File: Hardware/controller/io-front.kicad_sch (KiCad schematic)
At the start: 35 parts

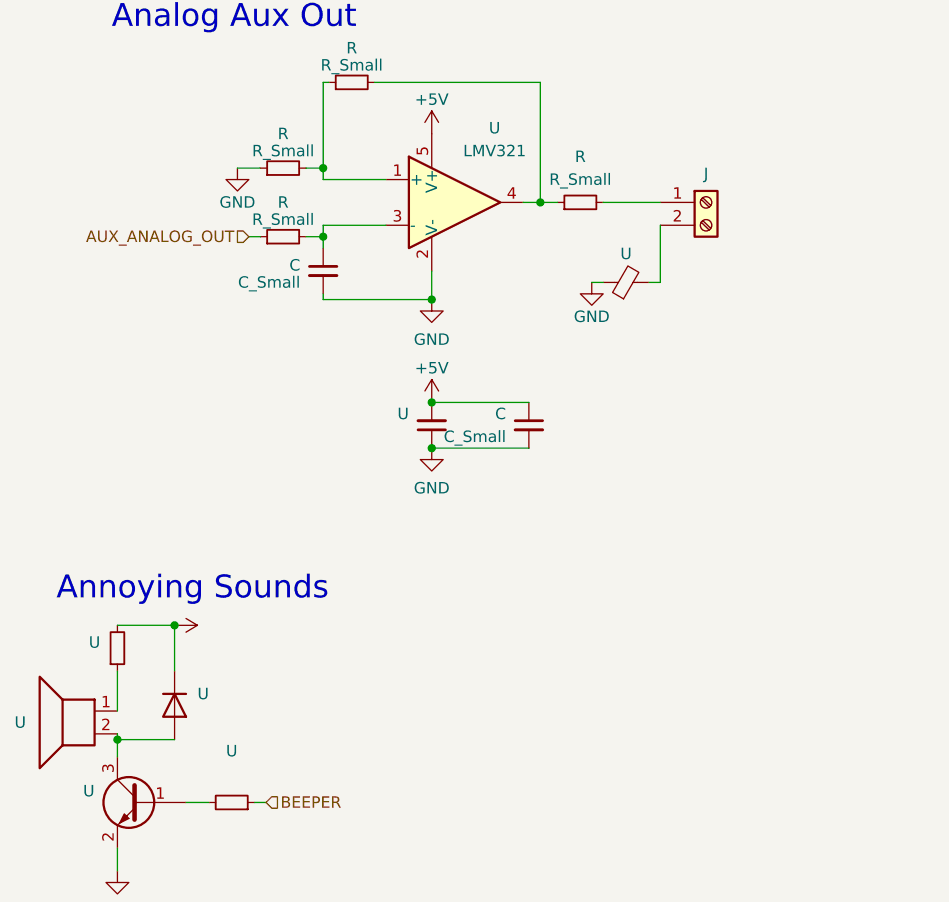
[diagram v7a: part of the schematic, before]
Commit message: hw: add more jlcpcb part numbers
- Switched a lot more passives around to use equivalent JLCPCB-available
  parts

- Slightly moved expansion power relay
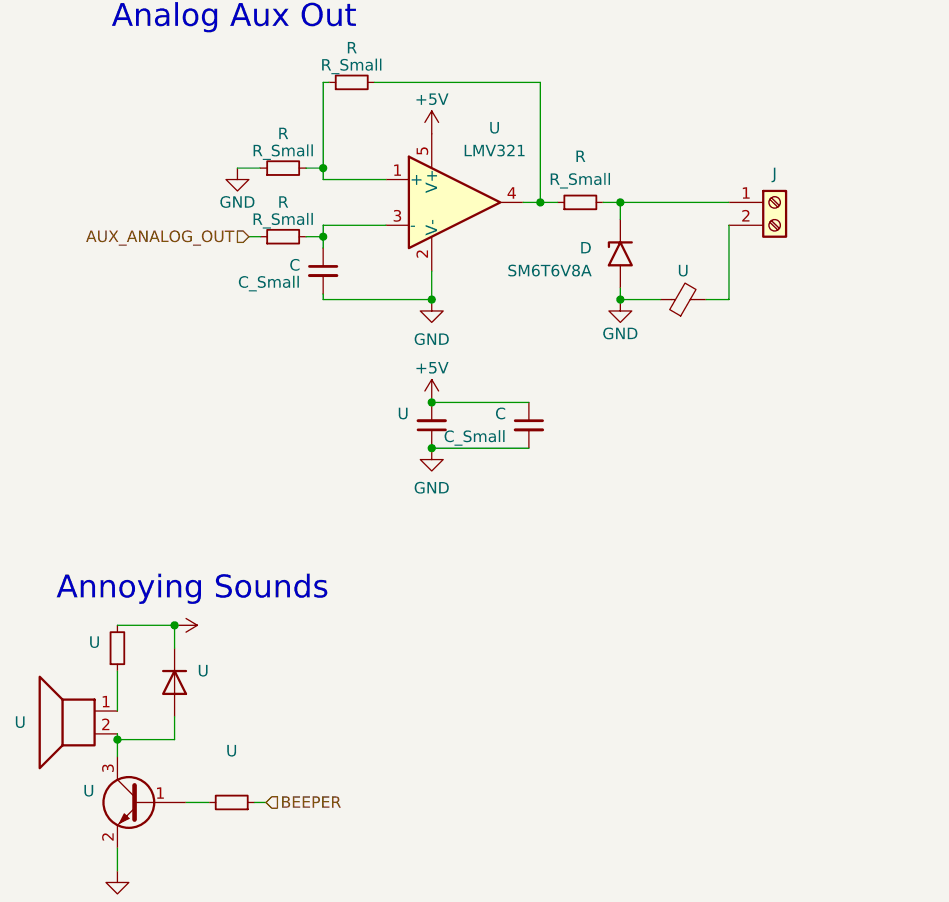
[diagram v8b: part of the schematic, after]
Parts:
- added D: SM6T6V8A, Diode_SMD:D_SMB, symbol Diode:SM6T6V8A
- U: MPN (none) -> CR0805-JW-102ELF
- U: JLCPCB (none) -> C64898; MPN FM4007W-W -> (none)
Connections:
- net GND: now also D.2 (A2)
- net at J.1 (Pin_1), R.2: now also D.1 (A1)
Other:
- moved on the sheet: J, U
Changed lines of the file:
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@@
   (junction (at 31.75 173.355) (diameter 0) (color 0 0 0 0)
+  )
+  (junction (at 164.465 125.095) (diameter 0) (color 0 0 0 0)
+  )
+  (junction (at 164.465 114.3) (diameter 0) (color 0 0 0 0)
   )
   (junction (at 114.935 161.29) (diameter 0) (color 0 0 0 0)
@@
     (stroke (width 0) (type default))
   )
-  (wire (pts (xy 168.91 116.84) (xy 168.91 123.19))
-    (stroke (width 0) (type default))
-  )
   (wire (pts (xy 131.445 111.76) (xy 131.445 110.49))
     (stroke (width 0) (type default))
@@
     (stroke (width 0) (type default))
   )
+  (wire (pts (xy 176.53 116.84) (xy 176.53 125.095))
+    (stroke (width 0) (type default))
+  )
   (wire (pts (xy 40.005 181.61) (xy 52.705 181.61))
     (stroke (width 0) (type default))
   )
+  (wire (pts (xy 162.56 114.3) (xy 164.465 114.3))
+    (stroke (width 0) (type default))
+  )
   (wire (pts (xy 31.75 173.355) (xy 31.75 165.1))
     (stroke (width 0) (type default))
   )
+  (wire (pts (xy 164.465 114.3) (xy 176.53 114.3))
+    (stroke (width 0) (type default))
+  )
   (bus (pts (xy 89.535 68.58) (xy 89.535 71.12))
     (stroke (width 0) (type default))
@@
     (stroke (width 0) (type default))
   )
+  (wire (pts (xy 168.91 125.095) (xy 164.465 125.095))
+    (stroke (width 0) (type default))
+  )
   (bus (pts (xy 89.535 48.26) (xy 89.535 50.8))
     (stroke (width 0) (type default))
@@
     (stroke (width 0) (type default))
   )
-  (wire (pts (xy 162.56 114.3) (xy 168.91 114.3))
-    (stroke (width 0) (type default))
-  )
   (wire (pts (xy 31.75 150.495) (xy 31.75 165.1))
     (stroke (width 0) (type default))
   )
-  (wire (pts (xy 168.91 123.19) (xy 167.64 123.19))
+  (wire (pts (xy 173.99 125.095) (xy 176.53 125.095))
     (stroke (width 0) (type default))
   )
@@
     (stroke (width 0) (type default))
   )
+  (wire (pts (xy 164.465 114.3) (xy 164.465 116.205))
+    (stroke (width 0) (type default))
+  )
   (wire (pts (xy 132.08 100.965) (xy 131.445 100.965))
     (stroke (width 0) (type default))
@@
     (stroke (width 0) (type default))
   )
+  (wire (pts (xy 114.935 171.45) (xy 114.935 173.99))
+    (stroke (width 0) (type default))
+  )
   (bus (pts (xy 89.535 83.82) (xy 89.535 86.36))
     (stroke (width 0) (type default))
@@
     (stroke (width 0) (type default))
   )
+  (wire (pts (xy 164.465 125.095) (xy 164.465 123.825))
+    (stroke (width 0) (type default))
+  )
   (bus (pts (xy 89.535 45.72) (xy 89.535 48.26))
     (stroke (width 0) (type default))
@@
     (stroke (width 0) (type default))
   )
-  (wire (pts (xy 161.29 123.19) (xy 162.56 123.19))
-    (stroke (width 0) (type default))
-  )
   (wire (pts (xy 139.7 36.83) (xy 165.1 36.83))
     (stroke (width 0) (type default))
@@
     (stroke (width 0) (type default))
   )
-  (wire (pts (xy 114.935 161.29) (xy 114.935 166.37))
+  (wire (pts (xy 114.935 161.29) (xy 114.935 163.83))
     (stroke (width 0) (type default))
   )
@@
       (effects (font (size 1.27 1.27)) hide)
     )
-    (property "MPN" "" (id 4) (at 221.615 33.655 0)
+    (property "MPN" "CR0805-JW-102ELF" (id 4) (at 221.615 33.655 0)
       (effects (font (size 1.27 1.27)) hide)
     )
@@
     (pin "2")
   )
-  (symbol (lib_id "Device:FerriteBead_Small") (at 165.1 123.19 90) (unit 1)
+  (symbol (lib_id "Device:FerriteBead_Small") (at 171.45 125.095 90) (unit 1)
     (in_bom yes) (on_board yes)
     (default_instance (reference "U") (unit 1) (value "") (footprint ""))
-    (property "Reference" "U" (id 0) (at 165.1 120.015 90)
-      (effects (font (size 1.27 1.27)))
-    )
-    (property "Value" "" (id 1) (at 165.0619 118.745 90)
-      (effects (font (size 1.27 1.27)) hide)
-    )
-    (property "Footprint" "" (id 2) (at 165.1 124.968 90)
-      (effects (font (size 1.27 1.27)) hide)
-    )
-    (property "Datasheet" "~" (id 3) (at 165.1 123.19 0)
-      (effects (font (size 1.27 1.27)) hide)
-    )
-    (property "MPN" "MFBM1V2012-800-R" (id 4) (at 165.1 123.19 90)
-      (effects (font (size 1.27 1.27)) hide)
-    )
-    (property "JLCPCB" "C1015" (id 5) (at 165.1 123.19 90)
+    (property "Reference" "U" (id 0) (at 171.45 121.92 90)
+      (effects (font (size 1.27 1.27)))
+    )
+    (property "Value" "" (id 1) (at 171.4119 120.65 90)
+      (effects (font (size 1.27 1.27)) hide)
+    )
+    (property "Footprint" "" (id 2) (at 171.45 126.873 90)
+      (effects (font (size 1.27 1.27)) hide)
+    )
+    (property "Datasheet" "~" (id 3) (at 171.45 125.095 0)
+      (effects (font (size 1.27 1.27)) hide)
+    )
+    (property "MPN" "MFBM1V2012-800-R" (id 4) (at 171.45 125.095 90)
+      (effects (font (size 1.27 1.27)) hide)
+    )
+    (property "JLCPCB" "C1015" (id 5) (at 171.45 125.095 90)
       (effects (font (size 1.27 1.27)) hide)
     )
@@
     (pin "1")
   )
+  (symbol (lib_id "Diode:SM6T6V8A") (at 164.465 120.015 90) (mirror x) (unit 1)
+    (in_bom yes) (on_board yes)
+    (default_instance (reference "D") (unit 1) (value "SM6T6V8A") (footprint "Diode_SMD:D_SMB"))
+    (property "Reference" "D" (id 0) (at 161.29 119.38 90)
+      (effects (font (size 1.27 1.27)) (justify left))
+    )
+    (property "Value" "SM6T6V8A" (id 1) (at 161.29 121.92 90)
+      (effects (font (size 1.27 1.27)) (justify left))
+    )
+    (property "Footprint" "Diode_SMD:D_SMB" (id 2) (at 169.545 120.015 0)
+      (effects (font (size 1.27 1.27)) hide)
+    )
+    (property "Datasheet" "https://www.st.com/resource/en/datasheet/sm6t.pdf" (id 3) (at 164.465 118.745 0)
+      (effects (font (size 1.27 1.27)) hide)
+    )
+    (property "JLCPCB" "C78395" (id 4) (at 164.465 120.015 90)
+      (effects (font (size 1.27 1.27)) hide)
+    )
+    (pin "1")
+    (pin "2")
+  )
   (symbol (lib_id "power:+3V3") (at 31.75 150.495 0) (unit 1)
     (in_bom yes) (on_board yes) (fields_autoplaced)
@@
     (pin "1")
   )
-  (symbol (lib_id "Connector:Screw_Terminal_01x02") (at 173.99 114.3 0) (unit 1)
+  (symbol (lib_id "Connector:Screw_Terminal_01x02") (at 181.61 114.3 0) (unit 1)
     (in_bom yes) (on_board yes)
     (default_instance (reference "J") (unit 1) (value "Screw_Terminal_01x02") (footprint ""))
-    (property "Reference" "J" (id 0) (at 173.99 111.125 0)
-      (effects (font (size 1.27 1.27)))
-    )
-    (property "Value" "Screw_Terminal_01x02" (id 1) (at 173.99 111.125 0)
-      (effects (font (size 1.27 1.27)) hide)
-    )
-    (property "Footprint" "" (id 2) (at 173.99 114.3 0)
-      (effects (font (size 1.27 1.27)) hide)
-    )
-    (property "Datasheet" "~" (id 3) (at 173.99 114.3 0)
-      (effects (font (size 1.27 1.27)) hide)
-    )
-    (property "MPN" "CUI_TBL002A-350-02GR-2OR" (id 4) (at 173.99 114.3 0)
+    (property "Reference" "J" (id 0) (at 181.61 111.125 0)
+      (effects (font (size 1.27 1.27)))
+    )
+    (property "Value" "Screw_Terminal_01x02" (id 1) (at 181.61 111.125 0)
+      (effects (font (size 1.27 1.27)) hide)
+    )
+    (property "Footprint" "" (id 2) (at 181.61 114.3 0)
+      (effects (font (size 1.27 1.27)) hide)
+    )
+    (property "Datasheet" "~" (id 3) (at 181.61 114.3 0)
+      (effects (font (size 1.27 1.27)) hide)
+    )
+    (property "MPN" "CUI_TBL002A-350-02GR-2OR" (id 4) (at 181.61 114.3 0)
       (effects (font (size 1.27 1.27)) hide)
     )
@@
       (effects (font (size 1.27 1.27)) hide)
     )
-    (property "MPN" "" (id 4) (at 221.615 28.575 0)
+    (property "MPN" "CR0805-JW-102ELF" (id 4) (at 221.615 28.575 0)
       (effects (font (size 1.27 1.27)) hide)
     )
@@
     (pin "2")
   )
-  (symbol (lib_id "Diode:SM4007") (at 114.935 170.18 270) (unit 1)
+  (symbol (lib_id "Diode:SM4007") (at 114.935 167.64 270) (unit 1)
     (in_bom yes) (on_board yes)
     (default_instance (reference "U") (unit 1) (value "") (footprint ""))
-    (property "Reference" "U" (id 0) (at 117.475 168.91 90)
+    (property "Reference" "U" (id 0) (at 117.475 166.37 90)
       (effects (font (size 1.27 1.27)) (justify left))
     )
-    (property "Value" "" (id 1) (at 117.475 171.45 90)
+    (property "Value" "" (id 1) (at 117.475 168.91 90)
       (effects (font (size 1.27 1.27)) (justify left))
     )
-    (property "Footprint" "" (id 2) (at 110.49 170.18 0)
-      (effects (font (size 1.27 1.27)) hide)
-    )
-    (property "Datasheet" "http://cdn-reichelt.de/documents/datenblatt/A400/SMD1N400%23DIO.pdf" (id 3) (at 114.935 170.18 0)
-      (effects (font (size 1.27 1.27)) hide)
-    )
-    (property "MPN" "FM4007W-W" (id 4) (at 114.935 170.18 90)
+    (property "Footprint" "" (id 2) (at 110.49 167.64 0)
+      (effects (font (size 1.27 1.27)) hide)
+    )
+    (property "Datasheet" "http://cdn-reichelt.de/documents/datenblatt/A400/SMD1N400%23DIO.pdf" (id 3) (at 114.935 167.64 0)
+      (effects (font (size 1.27 1.27)) hide)
+    )
+    (property "JLCPCB" "C64898" (id 5) (at 114.935 167.64 90)
       (effects (font (size 1.27 1.27)) hide)
     )
@@
     (pin "2")
   )
-  (symbol (lib_id "power:GND") (at 161.29 123.19 0) (unit 1)
+  (symbol (lib_id "power:GND") (at 164.465 125.095 0) (unit 1)
     (in_bom yes) (on_board yes)
     (default_instance (reference "#PWR") (unit 1) (value "GND") (footprint ""))
-    (property "Reference" "#PWR" (id 0) (at 161.29 129.54 0)
-      (effects (font (size 1.27 1.27)) hide)
-    )
-    (property "Value" "GND" (id 1) (at 161.29 127 0)
-      (effects (font (size 1.27 1.27)))
-    )
-    (property "Footprint" "" (id 2) (at 161.29 123.19 0)
-      (effects (font (size 1.27 1.27)) hide)
-    )
-    (property "Datasheet" "" (id 3) (at 161.29 123.19 0)
-      (effects (font (size 1.27 1.27)) hide)
-    )
+    (property "Reference" "#PWR" (id 0) (at 164.465 131.445 0)
+      (effects (font (size 1.27 1.27)) hide)
+    )
+    (property "Value" "GND" (id 1) (at 164.465 128.905 0)
+      (effects (font (size 1.27 1.27)))
+    )
+    (property "Footprint" "" (id 2) (at 164.465 125.095 0)
+      (effects (font (size 1.27 1.27)) hide)
+    )
+    (property "Datasheet" "" (id 3) (at 164.465 125.095 0)
+      (effects (font (size 1.27 1.27)) hide)
+    )
